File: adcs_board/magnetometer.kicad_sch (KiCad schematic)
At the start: 6 parts, among them U4 BM1422AGMV-ZE2

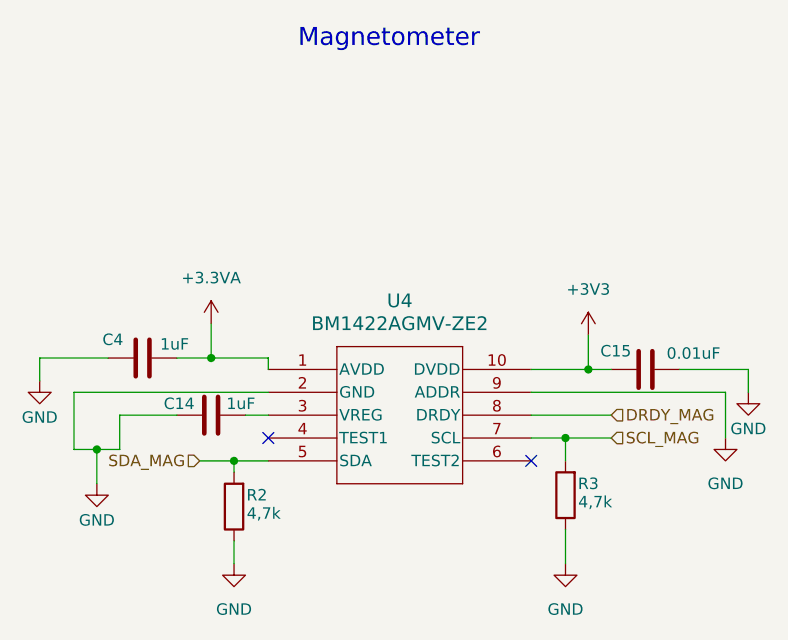
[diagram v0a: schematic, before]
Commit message: adcs_board: resolve schematic ERC violations
- Corrected electrical rule check (ERC) errors in ADCS BDOT schematic
- Fixed unconnected pins and mismatched power nets
- Adjusted symbol properties for proper ERC compliance
- Ensured clean schematic validation with no remaining ERC issues
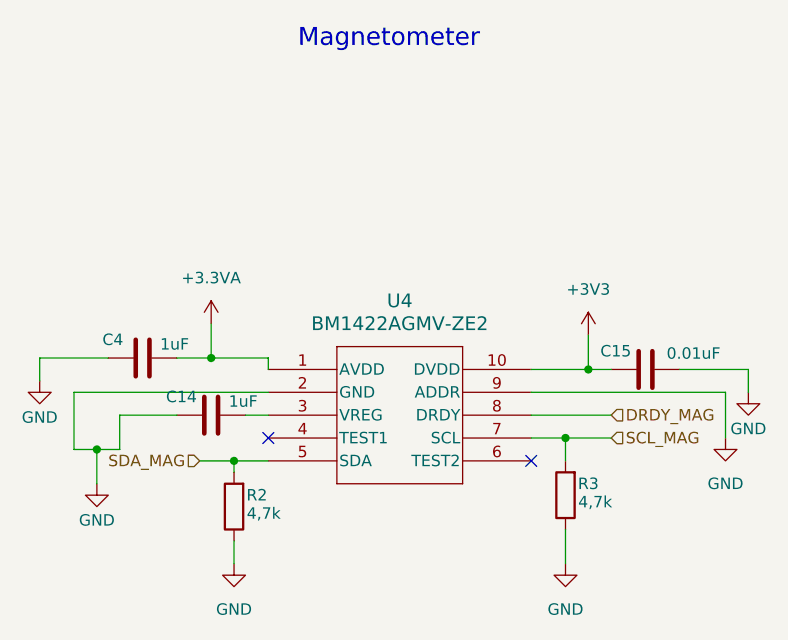
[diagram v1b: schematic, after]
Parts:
- C14, C4: footprint (none) -> Capacitor_SMD:C_0201_0603Metric; Manufacturer (none) -> Samsung Electro-Mechanics; Manufacturer Part Number (none) -> CL10B105KP8NNNC
- C15: footprint (none) -> Capacitor_SMD:C_0201_0603Metric; Manufacturer (none) -> KYOCERA AVX; Manufacturer Part Number (none) -> 06035C103MAZ2A
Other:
- title: (none) -> ADCS-BDOT
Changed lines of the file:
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@@
 	(generator_version "9.0")
 	(paper "A4")
+	(title_block
+		(title "ADCS-BDOT")
+		(rev "v0.1")
+		(comment 1 "Felipe C. Juliano <felipecostajuliano@live.com>")
+		(comment 2 "felipecostajuliano@live.com")
+	)
 	(text "Magnetometer\n"
 		(exclude_from_sim no)
@@
 			)
 		)
-		(property "Footprint" ""
+		(property "Footprint" "Capacitor_SMD:C_0201_0603Metric"
 			(at 111.76 88.5952 0)
 			(effects
@@
 			)
 		)
-		(property "Datasheet" "~"
+		(property "Datasheet" "https://mm.digikey.com/Volume0/opasdata/d220001/medias/docus/3584/CL10B105KP8NNNC_Spec.pdf"
 			(at 115.57 87.63 0)
 			(effects
@@
 			)
 		)
-		(property "Description" "Unpolarized capacitor"
+		(property "Description" "CAP CER 1UF 10V X7R 0603"
 			(at 115.57 87.63 0)
+			(effects
+				(font
+					(size 1.27 1.27)
+				)
+				(hide yes)
+			)
+		)
+		(property "Manufacturer" "Samsung Electro-Mechanics"
+			(at 115.57 87.63 90)
+			(effects
+				(font
+					(size 1.27 1.27)
+				)
+				(hide yes)
+			)
+		)
+		(property "Manufacturer Part Number" "CL10B105KP8NNNC"
+			(at 115.57 87.63 90)
 			(effects
 				(font
@@
 	(symbol
 		(lib_id "Device:C")
+		(at 123.19 93.98 270)
+		(unit 1)
+		(exclude_from_sim no)
+		(in_bom yes)
+		(on_board yes)
+		(dnp no)
+		(property "Reference" "C14"
+			(at 119.888 91.948 90)
+			(effects
+				(font
+					(size 1.27 1.27)
+				)
+			)
+		)
+		(property "Value" "1uF"
+			(at 126.746 92.456 90)
+			(effects
+				(font
+					(size 1.27 1.27)
+				)
+			)
+		)
+		(property "Footprint" "Capacitor_SMD:C_0201_0603Metric"
+			(at 119.38 94.9452 0)
+			(effects
+				(font
+					(size 1.27 1.27)
+				)
+				(hide yes)
+			)
+		)
+		(property "Datasheet" "https://mm.digikey.com/Volume0/opasdata/d220001/medias/docus/3584/CL10B105KP8NNNC_Spec.pdf"
+			(at 123.19 93.98 0)
+			(effects
+				(font
+					(size 1.27 1.27)
+				)
+				(hide yes)
+			)
+		)
+		(property "Description" "CAP CER 1UF 10V X7R 0603"
+			(at 123.19 93.98 0)
+			(effects
+				(font
+					(size 1.27 1.27)
+				)
+				(hide yes)
+			)
+		)
+		(property "Manufacturer" "Samsung Electro-Mechanics"
+			(at 123.19 93.98 90)
+			(effects
+				(font
+					(size 1.27 1.27)
+				)
+				(hide yes)
+			)
+		)
+		(property "Manufacturer Part Number" "CL10B105KP8NNNC"
+			(at 123.19 93.98 90)
+			(effects
+				(font
+					(size 1.27 1.27)
+				)
+				(hide yes)
+			)
+		)
+		(pin "2"
+		)
+		(pin "1"
+		)
+		(instances
+			(project "adcs_board"
+				(path "/28b5866e-000c-4f3b-b01c-a615d8361180/9d97a206-f6a8-4b23-88b0-be3df6e349fd"
+					(reference "C14")
+					(unit 1)
+				)
+			)
+		)
+	)
+	(symbol
+		(lib_id "Device:C")
 		(at 171.45 88.9 270)
 		(unit 1)
@@
 			)
 		)
-		(property "Footprint" ""
+		(property "Footprint" "Capacitor_SMD:C_0201_0603Metric"
 			(at 167.64 89.8652 0)
 			(effects
@@
 			)
 		)
-		(property "Datasheet" "~"
+		(property "Datasheet" "https://datasheets.kyocera-avx.com/KGF.pdf"
 			(at 171.45 88.9 0)
 			(effects
@@
 			)
 		)
-		(property "Description" "Unpolarized capacitor"
+		(property "Description" "CAP CER 0.01UF 50V X7R 0603"
 			(at 171.45 88.9 0)
+			(effects
+				(font
+					(size 1.27 1.27)
+				)
+				(hide yes)
+			)
+		)
+		(property "Manufacturer" "KYOCERA AVX"
+			(at 171.45 88.9 90)
+			(effects
+				(font
+					(size 1.27 1.27)
+				)
+				(hide yes)
+			)
+		)
+		(property "Manufacturer Part Number" "06035C103MAZ2A"
+			(at 171.45 88.9 90)
 			(effects
 				(font
@@
 					(unit 1)
 				)
-			)
-		)
-	)
-	(symbol
-		(lib_id "Device:C")
-		(at 123.19 93.98 270)
-		(unit 1)
-		(exclude_from_sim no)
-		(in_bom yes)
-		(on_board yes)
-		(dnp no)
-		(property "Reference" "C14"
-			(at 119.634 92.71 90)
-			(effects
-				(font
-					(size 1.27 1.27)
-				)
-			)
-		)
-		(property "Value" "1uF"
-			(at 126.492 92.71 90)
-			(effects
-				(font
-					(size 1.27 1.27)
-				)
-			)
-		)
-		(property "Footprint" ""
-			(at 119.38 94.9452 0)
-			(effects
-				(font
-					(size 1.27 1.27)
-				)
-				(hide yes)
-			)
-		)
-		(property "Datasheet" "~"
-			(at 123.19 93.98 0)
-			(effects
-				(font
-					(size 1.27 1.27)
-				)
-				(hide yes)
-			)
-		)
-		(property "Description" "Unpolarized capacitor"
-			(at 123.19 93.98 0)
-			(effects
-				(font
-					(size 1.27 1.27)
-				)
-				(hide yes)
-			)
-		)
-		(pin "2"
-		)
-		(pin "1"
-		)
-		(instances
-			(project "adcs_board"
-				(path "/28b5866e-000c-4f3b-b01c-a615d8361180/9d97a206-f6a8-4b23-88b0-be3df6e349fd"
-					(reference "C14")
-					(unit 1)
-				)
